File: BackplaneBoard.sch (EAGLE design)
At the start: 20 parts, among them U1 SN74CBTLV3257PWR, U2 SN74CBTLV3257PWR

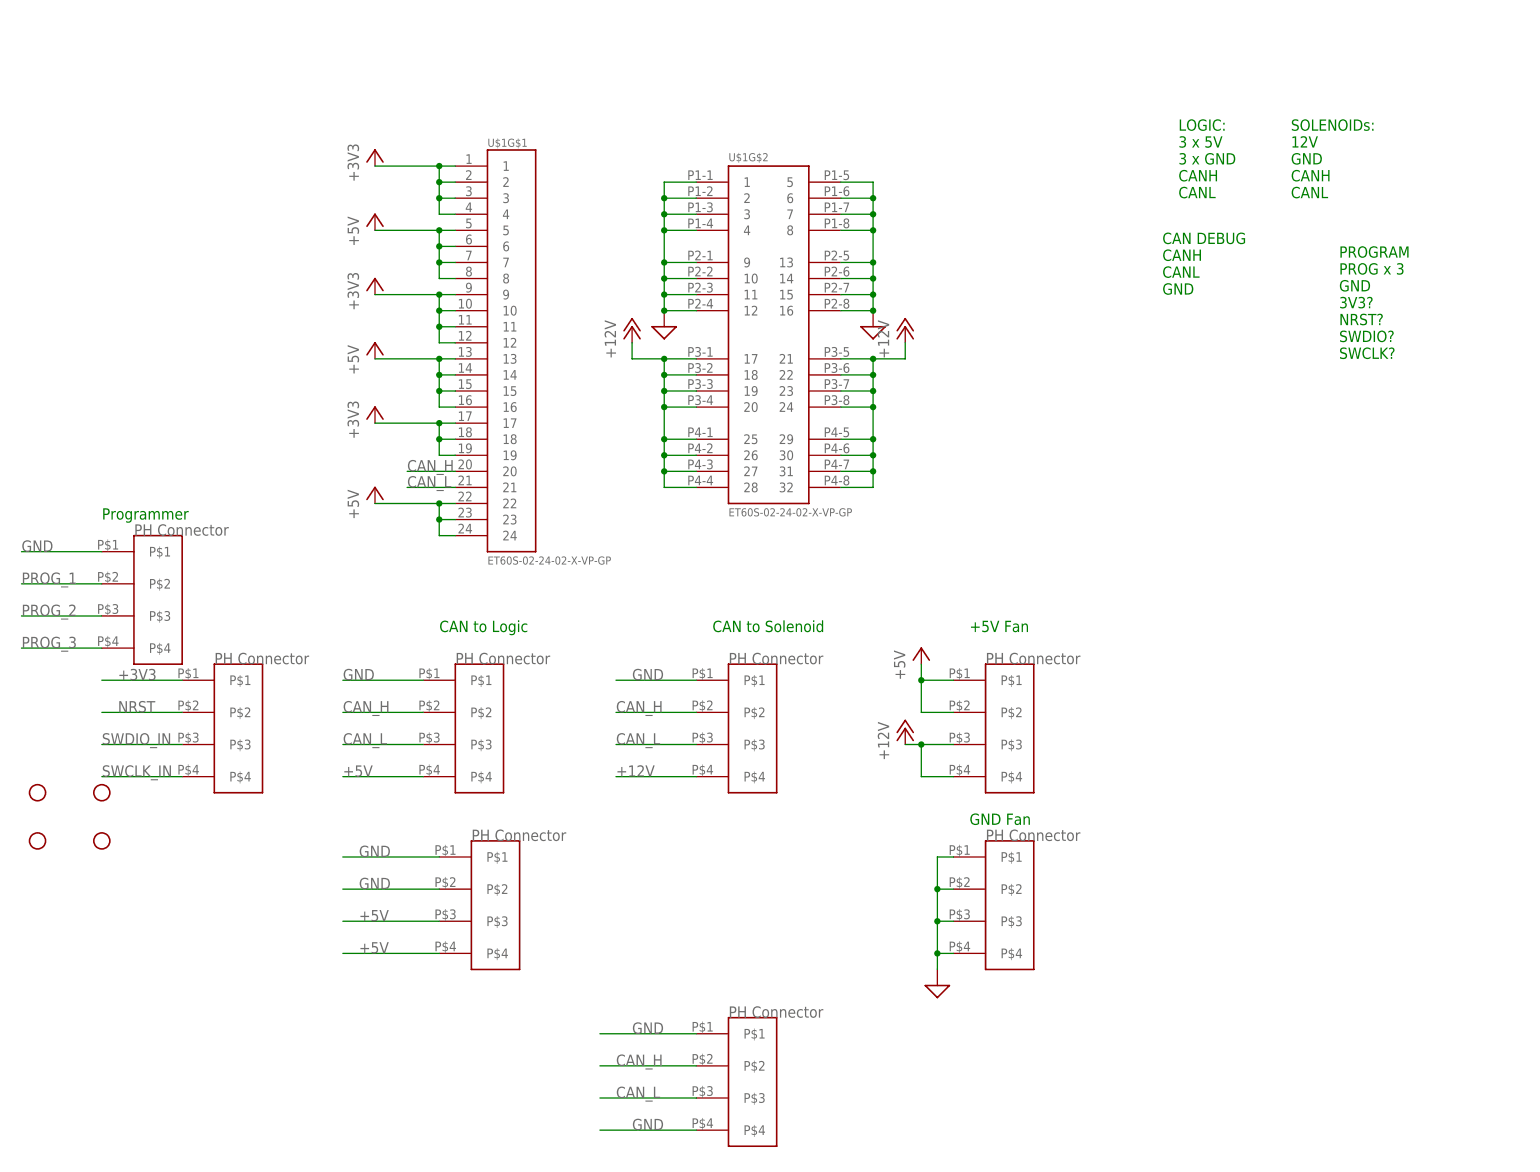
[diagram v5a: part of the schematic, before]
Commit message: added new te connectors
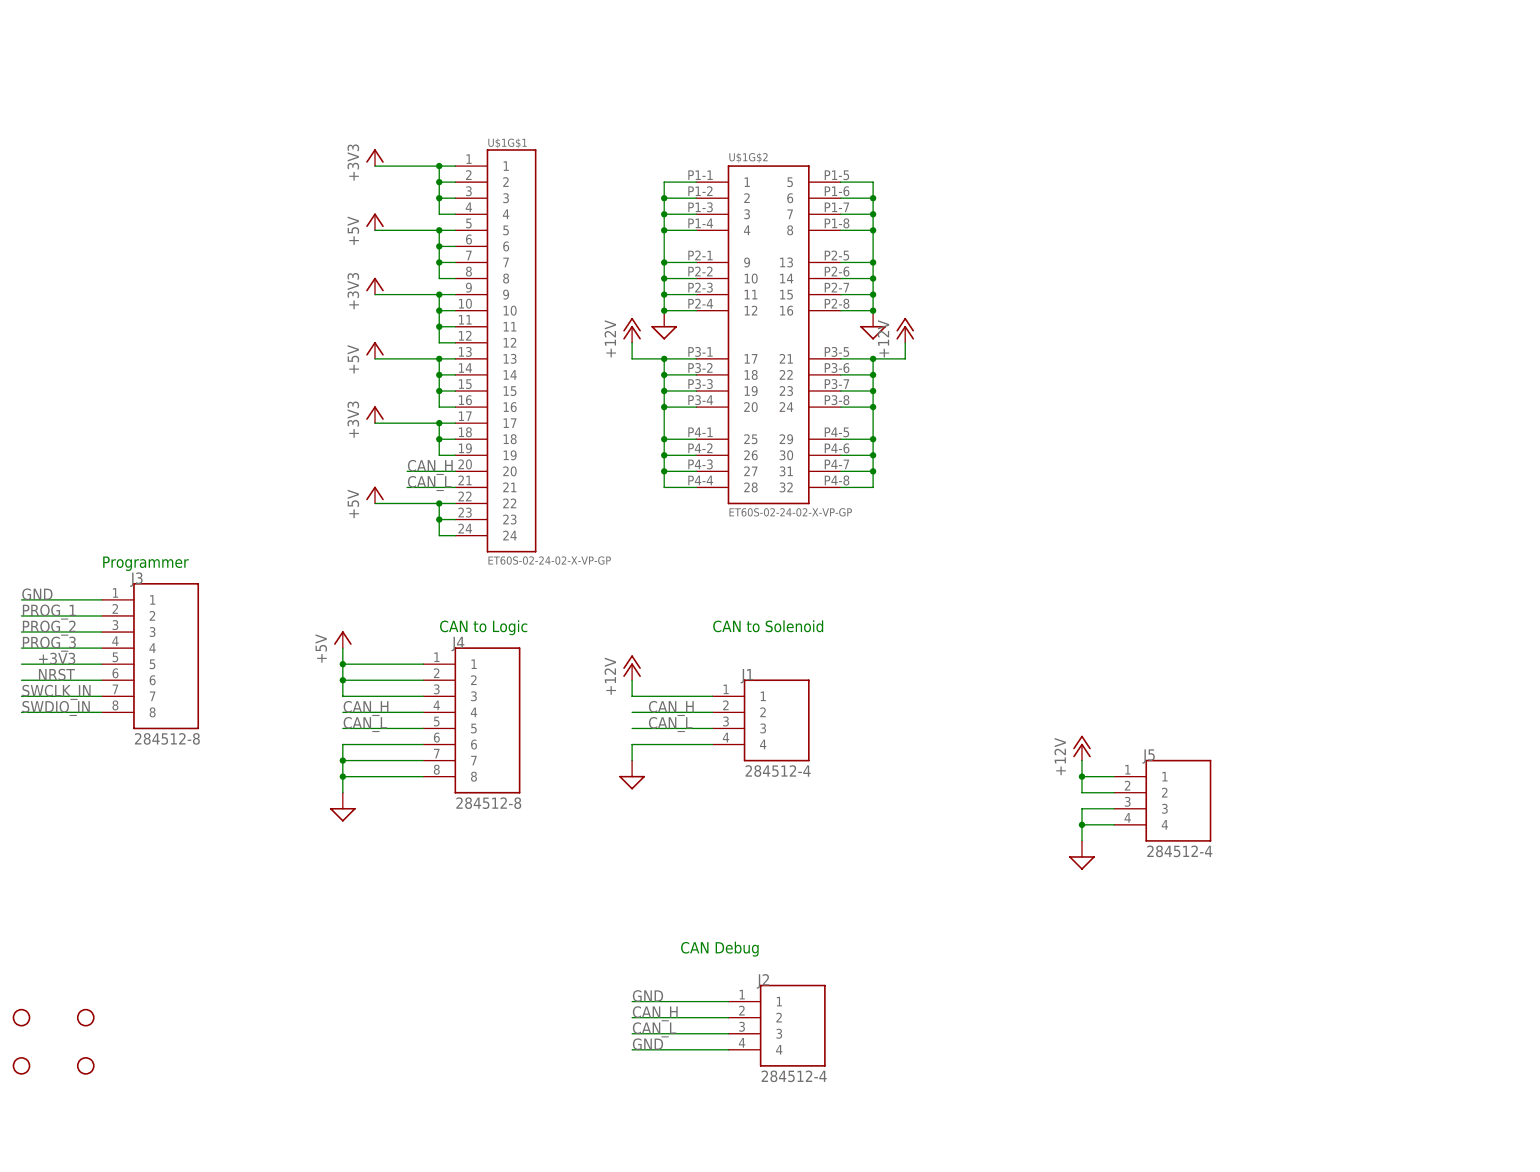
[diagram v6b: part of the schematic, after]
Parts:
- removed U$14, U$15, U$16, U$18, U$19, U$20, U$22, U$5: PHCONNECTOR, PHConnector:PHCONNECTOR
- added J1, J2, J5: 284512-4, 284512-4:284512-4
- added J3, J4: 284512-8, 284512-8:284512-8
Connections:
- net +12V: now also J1.1, J5.1, J5.2; no longer U$14.P$3, U$14.P$4, U$16.P$4
- net +3V3: now also J3.5; no longer U$22.P$1
- net +5V: now also J4.1, J4.2, J4.3; no longer U$14.P$1, U$14.P$2, U$19.P$4, U$20.P$3, U$20.P$4
- net CAN_H: now also J1.2, J2.2, J4.4; no longer U$16.P$2, U$18.P$2, U$19.P$2
- net CAN_L: now also J1.3, J2.3, J4.5; no longer U$16.P$3, U$18.P$3, U$19.P$3
- net GND: now also J1.4, J2.1, J2.4, J3.1, J4.6, J4.7, J4.8, J5.3, J5.4; no longer U$15.P$1, U$15.P$2, U$15.P$3, U$15.P$4, U$16.P$1, U$18.P$1, U$18.P$4, U$19.P$1, U$20.P$1, U$20.P$2, U$5.P$1
- net NRST: now also J3.6; no longer U$22.P$2
- net PROG_1: now also J3.2; no longer U$5.P$2
- net PROG_2: now also J3.3; no longer U$5.P$3
- net PROG_3: now also J3.4; no longer U$5.P$4
- net SWCLK_IN: now also J3.7; no longer U$22.P$4
- net SWDIO_IN: now also J3.8; no longer U$22.P$3
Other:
- note added: "CAN Debug"
- note removed: "+5V Fan"
- note removed: "CAN DEBUG CANH CANL GND"
- note removed: "GND Fan"
- note removed: "LOGIC: 3 x 5V 3 x GND CANH CANL"
- note removed: "PROGRAM PROG x 3 GND 3V3? NRST? SWDIO? SWCLK?"
- note removed: "SOLENOIDs: 12V GND CANH CANL"
